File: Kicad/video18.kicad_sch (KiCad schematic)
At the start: 18 parts, among them J201 DE15HD, U201 THS7316, U202 TPD7S019

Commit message: Update schematic files to Kicad 6.
Had to fix some symbols which didn't have perfect matches in K6.
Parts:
- renumbered C201 to C3001, C202 to C3002, C203 to C3003, C204 to C3004, C205 to C3005, C206 to C3006, J201 to J3001, R201 to R3001, R202 to R3002, R203 to R3003, R204 to R3004, R205 to R3005, R206 to R3006, R207 to R3007, R208 to R3008, R209 to R3009, U201 to U3001, U202 to U3002

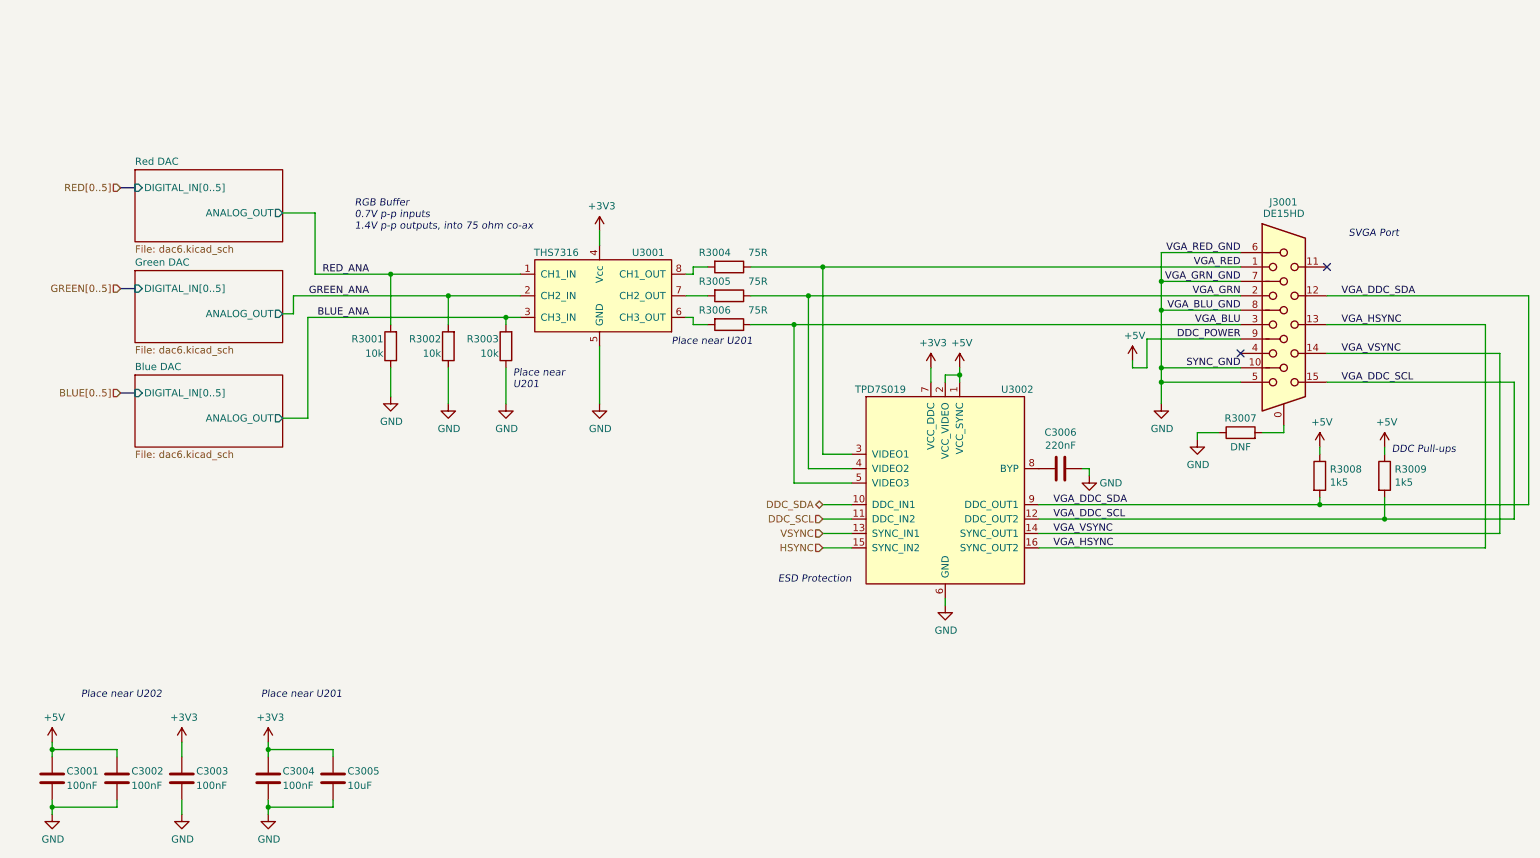
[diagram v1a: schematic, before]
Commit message: Imported sheets from Neotron Pico.
Standardised on +3V3 not +3.3V
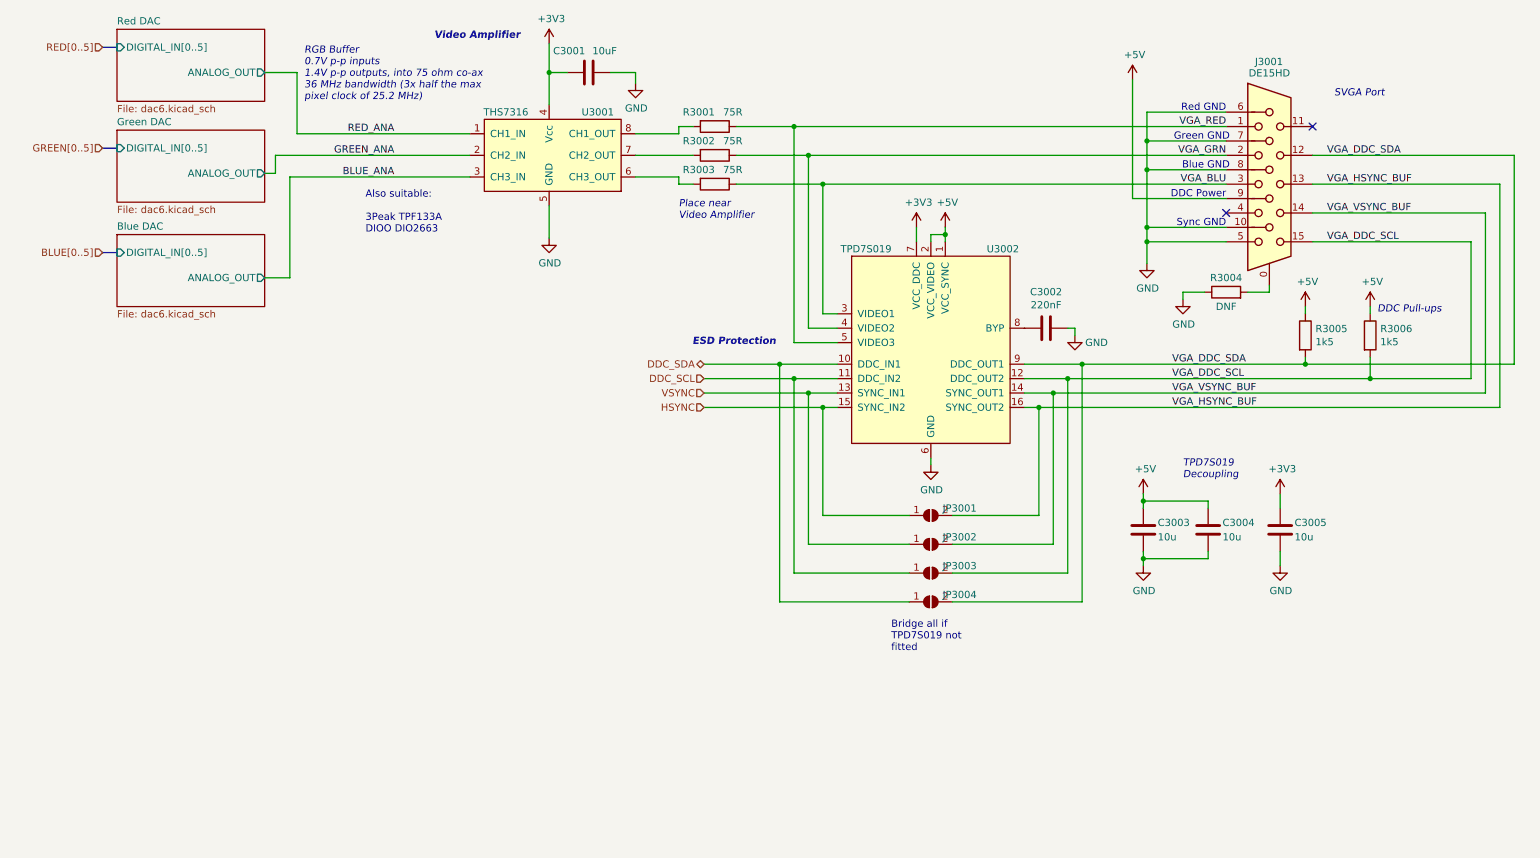
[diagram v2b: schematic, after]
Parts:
- removed C3006: 220nF, Capacitor_SMD:C_0805_2012Metric_Pad1.18x1.45mm_HandSolder, symbol Device:C
- removed R3007: DNF, Resistor_SMD:R_0805_2012Metric_Pad1.20x1.40mm_HandSolder, symbol Device:R
- removed R3008, R3009: 1k5, Resistor_SMD:R_0805_2012Metric_Pad1.20x1.40mm_HandSolder, symbol Device:R
- added JP3001, JP3002, JP3003, JP3004: Bridge, symbol Jumper:SolderJumper_2_Open
- C3001: value 100nF -> 10uF; Digikey BC1150CT-ND -> (none); JLCPCB Collection (none) -> Basic; LCSC Part# (none) -> C15850; MPN CPL-CAP-X7R-0805-100NF-50V -> CL21A106KAYNNNE; Manufacturer Vishay -> Samsung; Mouser 594-K104K15X7RF5TL2 -> (none); Voltage 16V -> 25V
- C3002: value 100nF -> 220nF; Digikey BC1150CT-ND -> (none); JLCPCB Collection (none) -> Basic; LCSC Part# (none) -> C5378; MPN CPL-CAP-X7R-0805-100NF-50V -> CL21B224KBFNNNE; Manufacturer Vishay -> Samsung; Mouser 594-K104K15X7RF5TL2 -> (none); Tolerance X5R -> X7R; Voltage 16V -> 50V
- C3003, C3004: value 100nF -> 10u; footprint Capacitor_SMD:C_0805_2012Metric_Pad1.18x1.45mm_HandSolder -> (none); Digikey BC1150CT-ND -> (none); JLCPCB Collection (none) -> Basic; LCSC Part# (none) -> C15850; MPN CPL-CAP-X7R-0805-100NF-50V -> CL21A106KAYNNNE; Manufacturer Vishay -> Samsung; Mouser 594-K104K15X7RF5TL2 -> (none); Voltage 10V -> 25V
- C3005: value 10uF -> 10u; footprint Capacitor_SMD:C_0805_2012Metric_Pad1.18x1.45mm_HandSolder -> (none); Digikey 1276-6455-1-ND -> (none); JLCPCB Collection (none) -> Basic; LCSC Part# (none) -> C15850; MPN CPL-CAP-X5R-0805-10UF-16V -> CL21A106KAYNNNE; Voltage 10V -> 25V
- R3001, R3002, R3003: value 10k -> 75R; Digikey RMCF0805FT10K0-ND -> (none); JLCPCB Collection (none) -> Basic; LCSC Part# (none) -> C20638; MPN CPL-RES-0805-10K-0.125W -> 0805W8F750JT5E; Manufacturer Stackpole -> Uniroyal
- R3004: value 75R -> DNF; DNP 0 -> 1; Digikey RMCF0805FT75R0-ND -> (none); MPN RMCF0805FT75R0 -> (none); Manufacturer Stackpole -> (none); Tolerance 1% -> (none)
- R3005, R3006: value 75R -> 1k5; Digikey RMCF0805FT75R0-ND -> (none); JLCPCB Collection (none) -> Basic; LCSC Part# (none) -> C17604; MPN RMCF0805FT75R0 -> 0805W8F2001T5E; Manufacturer Stackpole -> Uniroyal
- U3001: Digikey 296-26684-1-ND -> (none); JLCPCB Collection (none) -> Extended; LCSC Part# (none) -> C544774; MPN THS7316DR -> THS7316; Mouser 595-THS7316DR -> (none)
- U3002: Digikey 296-27595-1-ND -> (none); JLCPCB Collection (none) -> Extended; LCSC Part# (none) -> C337499; Mouser 595-TPD7S019-15DBQR -> (none)
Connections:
- net +3V3: now also C3001.1, C3005.2; no longer C3003.2, C3004.2, C3005.1
- net +5V: now also C3003.2, C3004.2, R3005.1, R3006.1; no longer C3001.2, C3002.2
- net BLUE_ANA: no longer R3003.2
- net DDC_SCL: now also JP3003.1 (A)
- net DDC_SDA: now also JP3004.1 (A)
- net GND: now also C3001.2, C3005.1, R3004.1; no longer C3001.1, C3005.2, R3001.1, R3002.1, R3003.1
- net GREEN_ANA: no longer R3002.2
- net HSYNC: now also JP3001.1 (A)
- net RED_ANA: no longer R3001.2
- net VGA_BLU: now also R3003.1, U3002.3 (VIDEO1); no longer R3006.1, U3002.5 (VIDEO3)
- net VGA_DDC_SCL: now also R3006.2, JP3003.2 (B)
- net VGA_DDC_SDA: now also R3005.2, JP3004.2 (B)
- net VGA_GRN: now also R3002.1; no longer R3005.1
- net VGA_RED: now also R3001.1, U3002.5 (VIDEO3); no longer R3004.1, U3002.3 (VIDEO1)
- net VSYNC: now also JP3002.1 (A)
- net at J3001.0: now also R3004.2
- net at U3001.8 (CH1_OUT): now also R3001.2; no longer R3004.2
- net at U3001.7 (CH2_OUT): now also R3002.2; no longer R3005.2
- net at U3001.6 (CH3_OUT): now also R3003.2; no longer R3006.2
- net at U3002.8 (BYP): now also C3002.2
- net VGA_HSYNC renamed VGA_HSYNC_BUF
- net VGA_HSYNC_BUF: now also JP3001.2 (B)
- net VGA_VSYNC renamed VGA_VSYNC_BUF
- net VGA_VSYNC_BUF: now also JP3002.2 (B)
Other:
- note added: "Also suitable: 3Peak TPF133A DIOO DIO2663"
- note added: "Blue GND"
- note added: "Bridge all if TPD7S019 not fitted"
- note added: "DDC Power"
- note added: "Green GND"
- note added: "Place near Video Amplifier"
- note added: "RGB Buffer 0.7V p-p inputs 1.4V p-p outputs, into 75 ohm co-ax 36 MHz bandwidth (3x half the max pixel clock of 25.2 MHz)"
- note added: "Red GND"
- note added: "Sync GND"
- note added: "TPD7S019 Decoupling"
- note added: "Video Amplifier"
- note removed: "Place near U201"
- note removed: "Place near U202"
- note removed: "RGB Buffer 0.7V p-p inputs 1.4V p-p outputs, into 75 ohm co-ax"

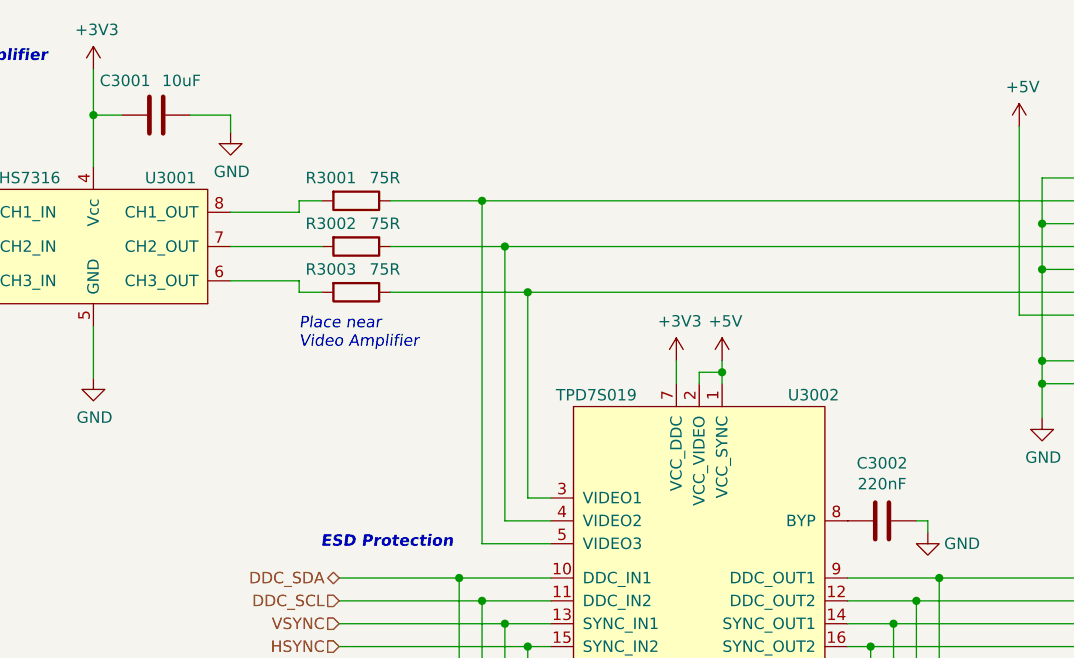
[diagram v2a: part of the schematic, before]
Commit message: Set missing footprints and update PCB
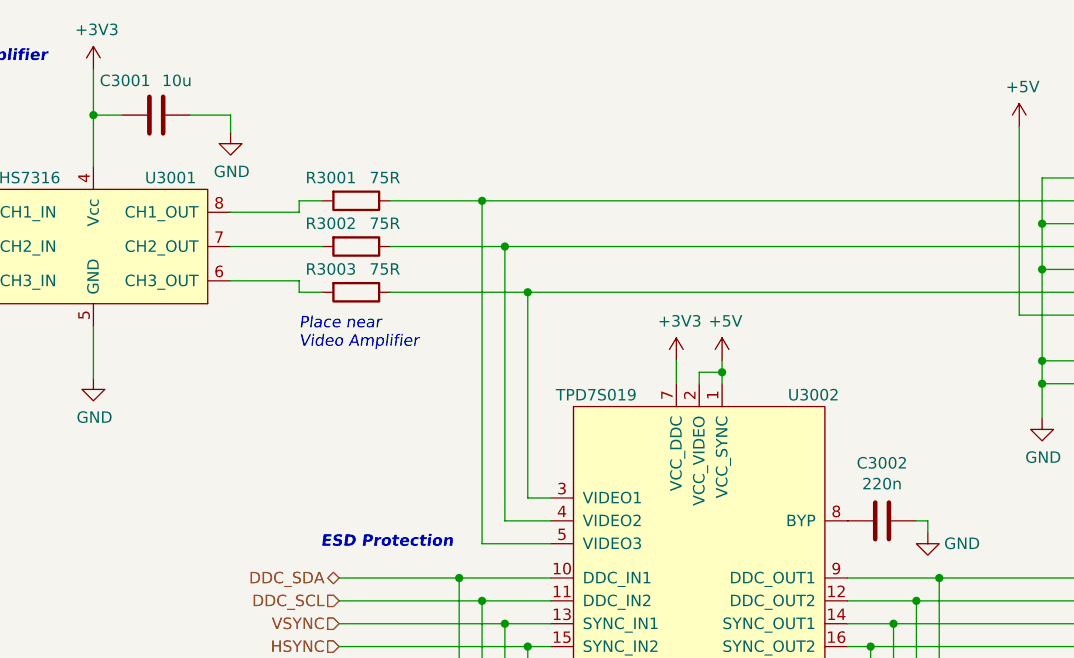
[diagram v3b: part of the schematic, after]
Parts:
- C3001: value 10uF -> 10u; JLCPCB Collection Basic -> (none); LCSC Part# C15850 -> (none); MPN CL21A106KAYNNNE -> (none); Manufacturer Samsung -> (none)
- C3002: value 220nF -> 220n
- C3003, C3004, C3005: footprint (none) -> Capacitor_SMD:C_0805_2012Metric_Pad1.18x1.45mm_HandSolder; JLCPCB Collection Basic -> (none); LCSC Part# C15850 -> (none); MPN CL21A106KAYNNNE -> (none); Manufacturer Samsung -> (none)
- JP3001, JP3002, JP3003, JP3004: footprint (none) -> Jumper:SolderJumper-2_P1.3mm_Open_RoundedPad1.0x1.5mm
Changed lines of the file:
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@@
       (effects (font (size 1.27 1.27)) (justify left))
     )
-    (property "Footprint" "" (id 2) (at 225.1202 133.985 0)
+    (property "Footprint" "Capacitor_SMD:C_0805_2012Metric_Pad1.18x1.45mm_HandSolder" (id 2) (at 225.1202 133.985 0)
       (effects (font (size 1.27 1.27)) hide)
     )
@@
       (effects (font (size 1.27 1.27)) hide)
     )
-    (property "Digikey" "~" (id 5) (at 224.155 137.795 0)
-      (effects (font (size 1.27 1.27)) hide)
-    )
-    (property "MPN" "CL21A106KAYNNNE" (id 6) (at 224.155 137.795 0)
-      (effects (font (size 1.27 1.27)) hide)
-    )
-    (property "Manufacturer" "Samsung" (id 7) (at 224.155 137.795 0)
-      (effects (font (size 1.27 1.27)) hide)
-    )
-    (property "LCSC Part#" "C15850" (id 8) (at 224.155 137.795 0)
+    (property "Digikey" "" (id 5) (at 224.155 137.795 0)
+      (effects (font (size 1.27 1.27)) hide)
+    )
+    (property "MPN" "" (id 6) (at 224.155 137.795 0)
+      (effects (font (size 1.27 1.27)) hide)
+    )
+    (property "Manufacturer" "" (id 7) (at 224.155 137.795 0)
+      (effects (font (size 1.27 1.27)) hide)
+    )
+    (property "LCSC Part#" "" (id 8) (at 224.155 137.795 0)
       (effects (font (size 1.27 1.27)) hide)
     )
@@
       (effects (font (size 1.27 1.27)) hide)
     )
-    (property "Mouser" "~" (id 11) (at 224.155 137.795 0)
-      (effects (font (size 1.27 1.27)) hide)
-    )
-    (property "JLCPCB Collection" "Basic" (id 12) (at 224.155 137.795 0)
+    (property "Mouser" "" (id 11) (at 224.155 137.795 0)
+      (effects (font (size 1.27 1.27)) hide)
+    )
+    (property "JLCPCB Collection" "" (id 12) (at 224.155 137.795 0)
       (effects (font (size 1.27 1.27)) hide)
     )
@@
       (effects (font (size 1.27 1.27)) hide)
     )
-    (property "Footprint" "" (id 2) (at 175.26 145.415 0)
+    (property "Footprint" "Jumper:SolderJumper-2_P1.3mm_Open_RoundedPad1.0x1.5mm" (id 2) (at 175.26 145.415 0)
       (effects (font (size 1.27 1.27)) hide)
     )
@@
       (effects (font (size 1.27 1.27)) (justify left))
     )
-    (property "Value" "10uF" (id 1) (at 115.57 53.34 90)
+    (property "Value" "10u" (id 1) (at 115.57 53.34 90)
       (effects (font (size 1.27 1.27)) (justify right))
     )
@@
       (effects (font (size 1.27 1.27)) hide)
     )
-    (property "Digikey" "~" (id 5) (at 114.935 57.15 0)
-      (effects (font (size 1.27 1.27)) hide)
-    )
-    (property "MPN" "CL21A106KAYNNNE" (id 6) (at 114.935 57.15 0)
-      (effects (font (size 1.27 1.27)) hide)
-    )
-    (property "Manufacturer" "Samsung" (id 7) (at 114.935 57.15 0)
-      (effects (font (size 1.27 1.27)) hide)
-    )
-    (property "LCSC Part#" "C15850" (id 8) (at 114.935 57.15 0)
+    (property "Digikey" "" (id 5) (at 114.935 57.15 0)
+      (effects (font (size 1.27 1.27)) hide)
+    )
+    (property "MPN" "" (id 6) (at 114.935 57.15 0)
+      (effects (font (size 1.27 1.27)) hide)
+    )
+    (property "Manufacturer" "" (id 7) (at 114.935 57.15 0)
+      (effects (font (size 1.27 1.27)) hide)
+    )
+    (property "LCSC Part#" "" (id 8) (at 114.935 57.15 0)
       (effects (font (size 1.27 1.27)) hide)
     )
@@
       (effects (font (size 1.27 1.27)) hide)
     )
-    (property "Mouser" "~" (id 11) (at 114.935 57.15 0)
-      (effects (font (size 1.27 1.27)) hide)
-    )
-    (property "JLCPCB Collection" "Basic" (id 12) (at 114.935 57.15 0)
+    (property "Mouser" "" (id 11) (at 114.935 57.15 0)
+      (effects (font (size 1.27 1.27)) hide)
+    )
+    (property "JLCPCB Collection" "" (id 12) (at 114.935 57.15 0)
       (effects (font (size 1.27 1.27)) hide)
     )
@@
     (in_bom yes) (on_board yes)
     (property "Reference" "C3002" (id 0) (at 195.58 95.8342 90))
-    (property "Value" "220nF" (id 1) (at 195.58 98.1456 90))
+    (property "Value" "220n" (id 1) (at 195.58 98.1456 90))
     (property "Footprint" "Capacitor_SMD:C_0805_2012Metric_Pad1.18x1.45mm_HandSolder" (id 2) (at 191.77 103.2002 0)
       (effects (font (size 1.27 1.27)) hide)
@@
       (effects (font (size 1.27 1.27)) hide)
     )
-    (property "Footprint" "" (id 2) (at 175.26 150.495 0)
+    (property "Footprint" "Jumper:SolderJumper-2_P1.3mm_Open_RoundedPad1.0x1.5mm" (id 2) (at 175.26 150.495 0)
       (effects (font (size 1.27 1.27)) hide)
     )
@@
       (effects (font (size 1.27 1.27)) (justify left))
     )
-    (property "Footprint" "" (id 2) (at 237.8202 133.985 0)
+    (property "Footprint" "Capacitor_SMD:C_0805_2012Metric_Pad1.18x1.45mm_HandSolder" (id 2) (at 237.8202 133.985 0)
       (effects (font (size 1.27 1.27)) hide)
     )
@@
       (effects (font (size 1.27 1.27)) hide)
     )
-    (property "Digikey" "~" (id 5) (at 236.855 137.795 0)
-      (effects (font (size 1.27 1.27)) hide)
-    )
-    (property "MPN" "CL21A106KAYNNNE" (id 6) (at 236.855 137.795 0)
-      (effects (font (size 1.27 1.27)) hide)
-    )
-    (property "Manufacturer" "Samsung" (id 7) (at 236.855 137.795 0)
-      (effects (font (size 1.27 1.27)) hide)
-    )
-    (property "LCSC Part#" "C15850" (id 8) (at 236.855 137.795 0)
+    (property "Digikey" "" (id 5) (at 236.855 137.795 0)
+      (effects (font (size 1.27 1.27)) hide)
+    )
+    (property "MPN" "" (id 6) (at 236.855 137.795 0)
+      (effects (font (size 1.27 1.27)) hide)
+    )
+    (property "Manufacturer" "" (id 7) (at 236.855 137.795 0)
+      (effects (font (size 1.27 1.27)) hide)
+    )
+    (property "LCSC Part#" "" (id 8) (at 236.855 137.795 0)
       (effects (font (size 1.27 1.27)) hide)
     )
@@
       (effects (font (size 1.27 1.27)) hide)
     )
-    (property "Mouser" "~" (id 11) (at 236.855 137.795 0)
-      (effects (font (size 1.27 1.27)) hide)
-    )
-    (property "JLCPCB Collection" "Basic" (id 12) (at 236.855 137.795 0)
+    (property "Mouser" "" (id 11) (at 236.855 137.795 0)
+      (effects (font (size 1.27 1.27)) hide)
+    )
+    (property "JLCPCB Collection" "" (id 12) (at 236.855 137.795 0)
       (effects (font (size 1.27 1.27)) hide)
     )
@@
       (effects (font (size 1.27 1.27)) hide)
     )
-    (property "Footprint" "" (id 2) (at 175.26 140.335 0)
+    (property "Footprint" "Jumper:SolderJumper-2_P1.3mm_Open_RoundedPad1.0x1.5mm" (id 2) (at 175.26 140.335 0)
       (effects (font (size 1.27 1.27)) hide)
     )
@@
       (effects (font (size 1.27 1.27)) (justify left))
     )
-    (property "Footprint" "" (id 2) (at 213.6902 133.985 0)
+    (property "Footprint" "Capacitor_SMD:C_0805_2012Metric_Pad1.18x1.45mm_HandSolder" (id 2) (at 213.6902 133.985 0)
       (effects (font (size 1.27 1.27)) hide)
     )
@@
       (effects (font (size 1.27 1.27)) hide)
     )
-    (property "Digikey" "~" (id 5) (at 212.725 137.795 0)
-      (effects (font (size 1.27 1.27)) hide)
-    )
-    (property "MPN" "CL21A106KAYNNNE" (id 6) (at 212.725 137.795 0)
-      (effects (font (size 1.27 1.27)) hide)
-    )
-    (property "Manufacturer" "Samsung" (id 7) (at 212.725 137.795 0)
-      (effects (font (size 1.27 1.27)) hide)
-    )
-    (property "LCSC Part#" "C15850" (id 8) (at 212.725 137.795 0)
+    (property "Digikey" "" (id 5) (at 212.725 137.795 0)
+      (effects (font (size 1.27 1.27)) hide)
+    )
+    (property "MPN" "" (id 6) (at 212.725 137.795 0)
+      (effects (font (size 1.27 1.27)) hide)
+    )
+    (property "Manufacturer" "" (id 7) (at 212.725 137.795 0)
+      (effects (font (size 1.27 1.27)) hide)
+    )
+    (property "LCSC Part#" "" (id 8) (at 212.725 137.795 0)
       (effects (font (size 1.27 1.27)) hide)
     )
@@
       (effects (font (size 1.27 1.27)) hide)
     )
-    (property "Mouser" "~" (id 11) (at 212.725 137.795 0)
-      (effects (font (size 1.27 1.27)) hide)
-    )
-    (property "JLCPCB Collection" "Basic" (id 12) (at 212.725 137.795 0)
+    (property "Mouser" "" (id 11) (at 212.725 137.795 0)
+      (effects (font (size 1.27 1.27)) hide)
+    )
+    (property "JLCPCB Collection" "" (id 12) (at 212.725 137.795 0)
       (effects (font (size 1.27 1.27)) hide)
     )
@@
       (effects (font (size 1.27 1.27)) hide)
     )
-    (property "Footprint" "" (id 2) (at 175.26 135.255 0)
-      (effects (font (size 1.27 1.27)) hide)
-    )
+    (property "Footprint" "Jumper:SolderJumper-2_P1.3mm_Open_RoundedPad1.0x1.5mm" (id 2) (at 175.26 135.255 0)
+      (effects (font (size 1.27 1.27)) hide)
+    )
